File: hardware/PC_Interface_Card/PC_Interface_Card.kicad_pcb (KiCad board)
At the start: 2 copper layers, 69 parts, among them J1 GSB1C41110SSHR, J2 Conn_01x10_Pin, J3 DM3BT-DSF-PEJS, Q1 PMOS, SW1 B3W-900-1, SW2 B3W-900-1, SW3 B3W-900-1, SW4 B3W-900-1, SW5 B3W-900-1, SW6 TL1240YQ2JBLK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

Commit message: footprint and 3d model fixes, footprint mismatch persists for B3W-9000 still. Need a fix.
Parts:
- SW1, SW2, SW3, SW4, SW5: footprint Footprint:B3W-900-1_OMR -> Footprint:SW6_B3W-9-1_OMR
- moved SW1 9.30 mm to (21.7, 23.6)
- moved SW2 9.30 mm to (21.7, 37.5)
- moved SW3 9.30 mm to (21.7, 51.4)
- moved SW4 9.30 mm to (21.7, 65.2)
- moved SW5 9.30 mm to (21.7, 79.1)

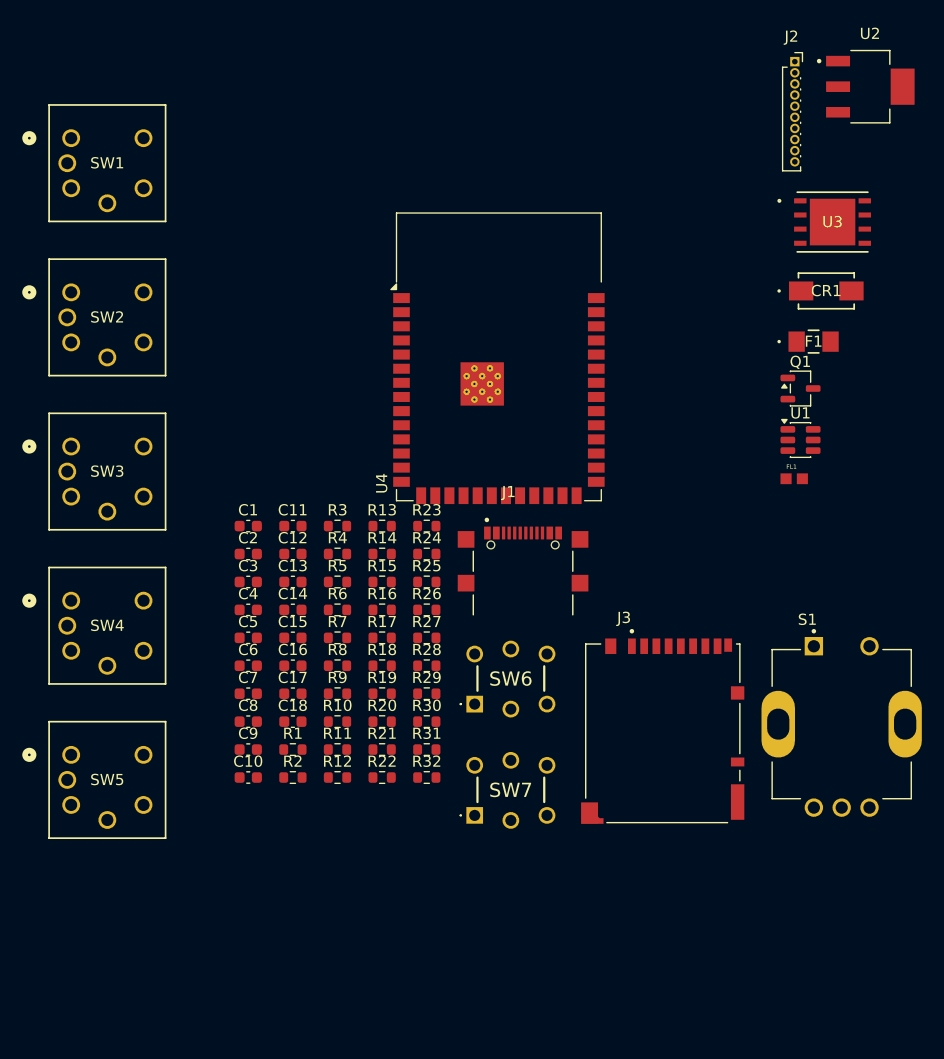
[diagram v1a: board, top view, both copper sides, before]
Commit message: Footprints added with BoM update and all 3d models added.
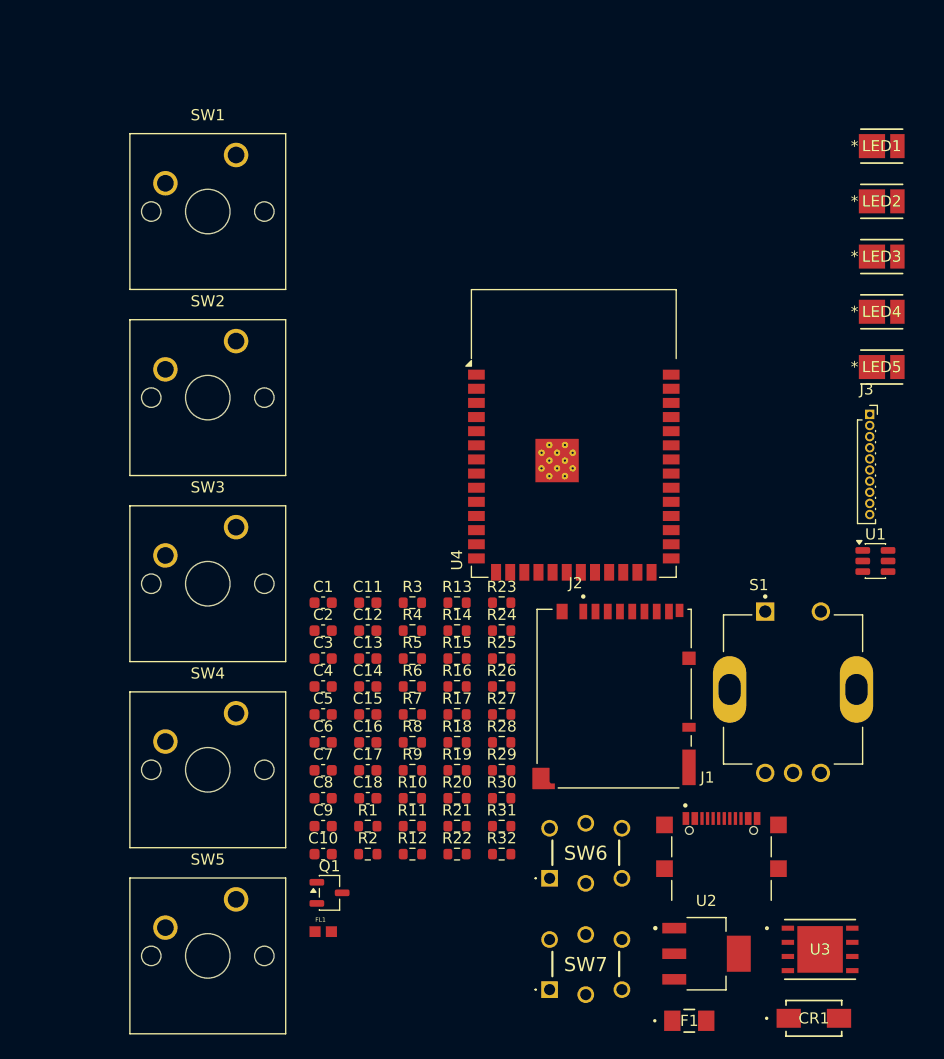
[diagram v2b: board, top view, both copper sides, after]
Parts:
- added LED1: LED_Cree_JE2835, Footprint:LED_JE2835_CRW-M, F.Cu at (94.5, 24.4)
- added LED2: LED_Cree_JE2835, Footprint:LED_JE2835_CRW-M, F.Cu at (94.5, 29.3)
- added LED3: LED_Cree_JE2835, Footprint:LED_JE2835_CRW-M, F.Cu at (94.5, 34.3)
- added LED4: LED_Cree_JE2835, Footprint:LED_JE2835_CRW-M, F.Cu at (94.5, 39.3)
- added LED5: LED_Cree_JE2835, Footprint:LED_JE2835_CRW-M, F.Cu at (94.5, 44.2)
- C10, C14, C5: value 1u_16V_0603 -> 100n_16V_0603
- C13, C16, C3: value 100n_16V_0603 -> 1u_16V_0603
- J2: value Conn_01x10_Pin -> DM3BT-DSF-PEJS; footprint Connector_PinSocket_1.00mm:PinSocket_1x10_P1.00mm_Vertical -> Footprint_Project_PC_Interface:HRS_DM3BT-DSF-PEJS
- J3: value DM3BT-DSF-PEJS -> Conn_01x10_Pin; footprint Footprint_Project_PC_Interface:HRS_DM3BT-DSF-PEJS -> Connector_PinSocket_1.00mm:PinSocket_1x10_P1.00mm_Vertical
- R10, R9: value 5.1k_0.2W_0603 -> 10k_0.2W_0603
- R13, R14, R16, R20, R21, R24: value 68R_0.2W_0603 -> 10k_0.2W_0603
- R17, R19, R22, R23, R26: value 10k_0.2W_0603 -> 33R_0.2W_0603
- R2: value 4R7_0.2W_0603 -> 10k_0.2W_0603
- R27: value 10k_0.2W_0603 -> 68R_0.2W_0603
- R6, R7: value 10k_0.2W_0603 -> 5.1k_0.2W_0603
- R8: value 10k_0.2W_0603 -> 4R7_0.2W_0603
- SW1, SW2, SW3, SW4, SW5: value B3W-900-1 -> CherryMX; footprint Footprint:SW6_B3W-9-1_OMR -> CherryMX_PCB:CherryMX_1.00u_PCB
- moved U2 79.3 mm to (78.8, 96.9)
- moved CR1 65.4 mm to (88.4, 102.7)
- moved U3 65.4 mm to (89.0, 96.5)
- moved F1 62.0 mm to (77.2, 103.0)
- moved Q1 62.0 mm to (44.9, 91.5)
- moved FL1 58.7 mm to (44.3, 94.9)
- moved J2 52.7 mm to (70.5, 66.9)
- moved J1 31.2 mm to (80.1, 88.5)
- moved J3 28.5 mm to (93.4, 48.5)
- moved SW5 21.8 mm to (34.0, 97.1)
- moved SW4 19.5 mm to (34.0, 80.4)
- moved SW3 17.4 mm to (34.0, 63.7)
- moved SW6 17.0 mm to (64.7, 90.2)
- moved SW7 17.0 mm to (64.7, 100.2)
- moved SW2 15.5 mm to (34.0, 47.0)
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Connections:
- C10 pad 1: VCC -> ENC_A
- C11 pad 1: VCC -> ENC_B
- C12 pad 1: SW_EN -> SW_MENU
- C13 pad 1: ENC_SW -> VCC
- C14 pad 1: VCC -> SW_EN
- C16 pad 1: SW_BOOT -> VCC
- C17 pad 1: ENC_A -> SW_BOOT
- C18 pad 1: ENC_B -> VCC
- C3 pad 1: SW_LEFT -> VLDO
- C4 pad 1: SW_UP -> VLDO
- C5 pad 1: VLDO -> SW_LEFT
- C6 pad 1: VLDO -> SW_UP
- C7 pad 1: SW_MENU -> ENC_SW
- J2 pad 1: VCC -> D2_SDMMC
- J2 pad 2: DC_DISP -> D3_SDMMC
- J2 pad 3: CS_DISP -> CMD_SDMMC
- J2 pad 4: MOSI -> VCC
- J2 pad 5: SCLK -> CLK_SDMMC
- J2 pad 6: MISO -> GND
- J2 pad 7: RST_DISP -> D0_SDMMC
- J2 pad 8: LED_DISP -> D1_SDMMC
- J3 pad 1: D2_SDMMC -> VCC
- J3 pad 2: D3_SDMMC -> DC_DISP
- J3 pad 3: CMD_SDMMC -> CS_DISP
- J3 pad 4: VCC -> MOSI
- J3 pad 5: CLK_SDMMC -> SCLK
- J3 pad 6: GND -> MISO
- J3 pad 7: D0_SDMMC -> RST_DISP
- J3 pad 8: D1_SDMMC -> LED_DISP
- R10 pad 1: CC2 -> RST_DISP
- R10 pad 2: GND -> VCC
- R13 pad 1: Net-(SW1-ANODE) -> ENC_SW
- R14 pad 1: Net-(SW2-ANODE) -> SW_RIGHT
- R15 pad 1: SW_MENU -> SW_DN
- R16 pad 1: Net-(SW3-ANODE) -> Net-(U3-*WP)
- R17 pad 1: Net-(U3-*WP) -> Net-(LED1-Pad2)
- R18 pad 1: SW_RIGHT -> ENC_A
- R19 pad 1: SW_DN -> Net-(LED2-Pad2)
- R2 pad 1: LED_DISP -> D1_SDMMC
- R2 pad 2: Net-(Q1-D) -> VCC
- R20 pad 1: Net-(SW4-ANODE) -> ENC_B
- R21 pad 1: Net-(SW5-ANODE) -> SW_MENU
- R22 pad 1: GND -> Net-(LED3-Pad2)
- R22 pad 2: Net-(U3-*RESET) -> VCC
- R23 pad 1: SW_EN -> Net-(LED4-Pad2)
- R24 pad 1: Net-(SW6-+) -> GND
- R24 pad 2: VCC -> Net-(U3-*RESET)
- R25 pad 1: ENC_SW -> SW_EN
- R26 pad 1: GND -> Net-(LED5-Pad2)
- R26 pad 2: Net-(U4-IO3) -> VCC
- R27 pad 1: ENC_A -> Net-(SW6-+)
- R28 pad 1: SW_BOOT -> GND
- R28 pad 2: VCC -> Net-(U4-IO3)
- R29 pad 1: ENC_B -> SW_BOOT
- R3 pad 1: D1_SDMMC -> D2_SDMMC
- R4 pad 1: D2_SDMMC -> D3_SDMMC
- R5 pad 1: D3_SDMMC -> CMD_SDMMC
- R6 pad 1: GND -> CC1
- R6 pad 2: PWM_DISP -> GND
- R7 pad 1: CMD_SDMMC -> CC2
- R7 pad 2: VCC -> GND
- R8 pad 1: RST_DISP -> LED_DISP
- R8 pad 2: VCC -> Net-(Q1-D)
- R9 pad 1: CC1 -> GND
- R9 pad 2: GND -> PWM_DISP
- SW1 pad 2: SW_LEFT -> GND
- SW2 pad 2: SW_UP -> GND
- SW3 pad 1: SW_MENU -> SW_RIGHT
- SW3 pad 2: SW_MENU -> GND
- SW4 pad 1: SW_RIGHT -> SW_DN
- SW4 pad 2: SW_RIGHT -> GND
- SW5 pad 1: SW_DN -> SW_MENU
- SW5 pad 2: SW_DN -> GND

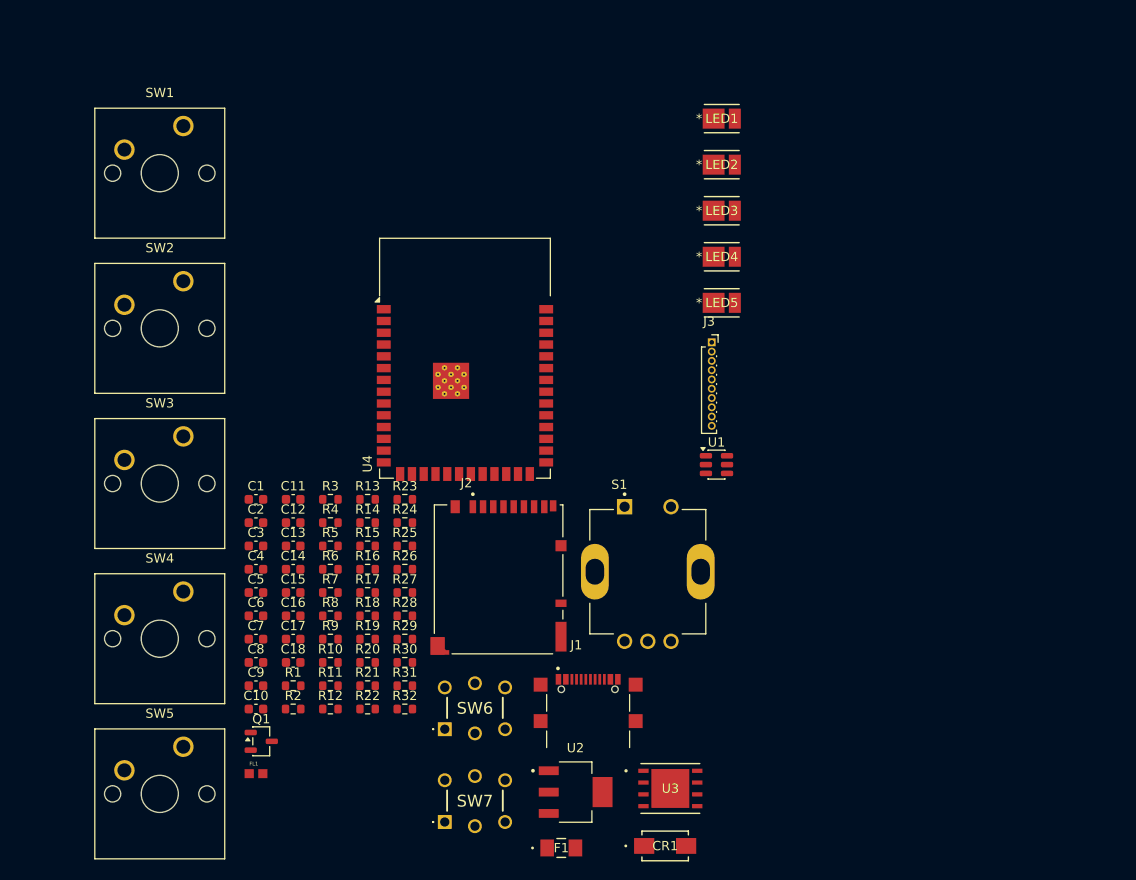
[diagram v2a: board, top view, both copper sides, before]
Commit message: More BoM fixes and 3D models, off board parts added.
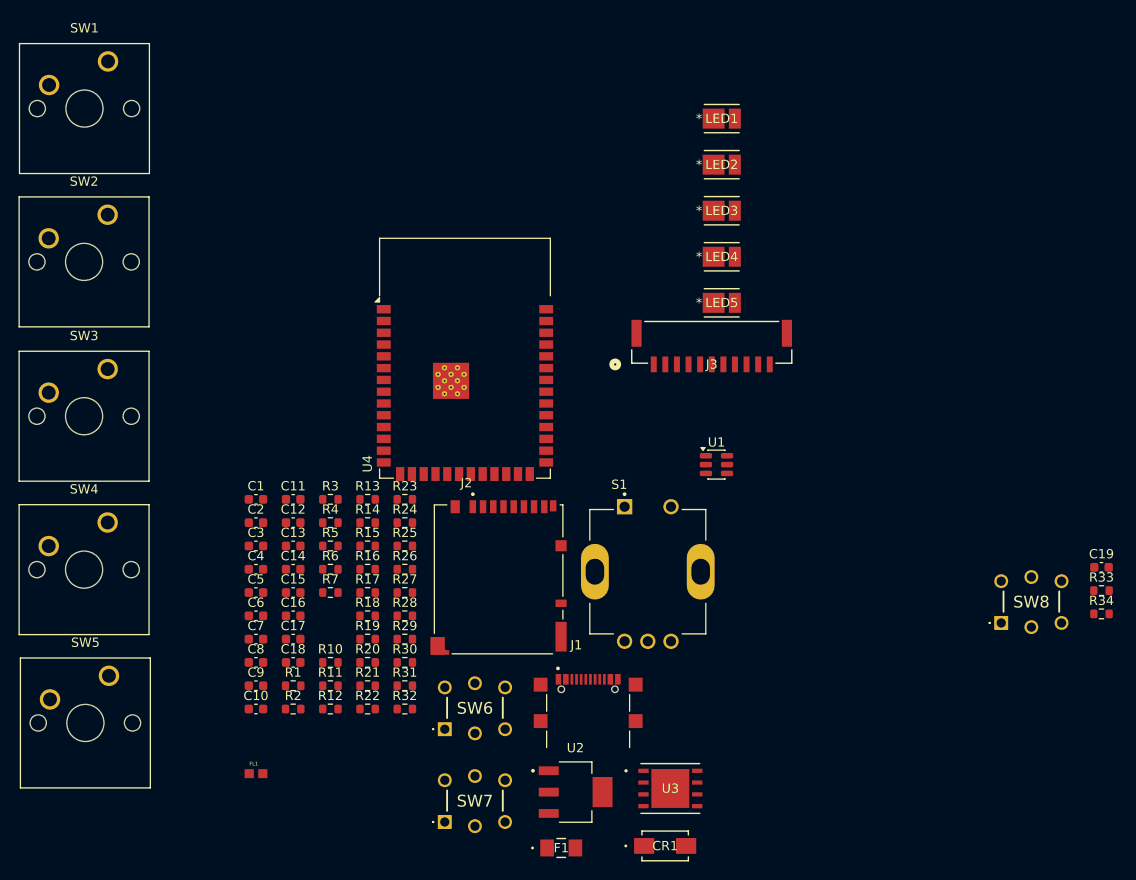
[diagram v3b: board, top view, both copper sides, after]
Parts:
- removed Q1: PMOS, Package_TO_SOT_SMD:SOT-23-3
- removed R8: 4R7_0.2W_0603, Resistor_SMD:R_0603_1608Metric
- removed R9: 10k_0.2W_0603, Resistor_SMD:R_0603_1608Metric
- added C19: 100n_16V_0603, Capacitor_SMD:C_0603_1608Metric, F.Cu at (135.4, 72.7)
- added R33: 10k_0.2W_0603, Resistor_SMD:R_0603_1608Metric, F.Cu at (135.4, 75.2)
- added R34: 68R_0.2W_0603, Resistor_SMD:R_0603_1608Metric, F.Cu at (135.4, 77.7)
- added SW8: TL1240YQ2JBLK, Footprint:TL1240YQ, F.Cu at (124.6, 78.7)
- J3: value Conn_01x10_Pin -> BM11B-GHS-TBT; footprint Connector_PinSocket_1.00mm:PinSocket_1x10_P1.00mm_Vertical -> Footprint_Project_PC_Interface:CONN11_BM11B-GHS-TBTLFSNN_JST
- moved SW5 11.1 mm to (25.9, 89.5)
- moved SW4 11.0 mm to (25.8, 73.0)
- moved SW3 10.9 mm to (25.8, 56.4)
- moved SW2 10.9 mm to (25.8, 39.8)
- moved SW1 10.7 mm to (25.9, 23.3)
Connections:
- J3 pad 2: DC_DISP -> GND
- J3 pad 3: CS_DISP -> MISO
- J3 pad 6: MISO -> CS_DISP
- J3 pad 7: RST_DISP -> DC_DISP
- J3 pad 8: LED_DISP -> RST_DISP
- J3 pad 9: GND -> PWM_DISP

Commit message: Changed encoder to a right angle one
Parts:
- removed S1: PEC11R-4120K-S0018, Footprint:XDCR_PEC11R-4120K-S0018
- added MT1: ACZ11BR1E-15KQA1-12C, Footprint:XDCR_ACZ11BR1E-15KQA1-12C, F.Cu at (231.2, 33.9)
- moved U2 113.1 mm to (13.4, 4.64)
- moved U4 107.0 mm to (167.2, 13.2)
- moved SW6 105.2 mm to (168.9, 104.6)
- moved U3 104.6 mm to (-3.50, 47.7)
- moved J3 92.7 mm to (185.1, 62.4)
- moved CR1 92.1 mm to (-3.14, 92.6)
- moved U1 90.9 mm to (26.2, 1.04)
- moved F1 84.8 mm to (-2.98, 75.5)
- moved C1 82.9 mm to (45.5, -17.5)
- moved C11 82.9 mm to (49.5, -17.5)
- moved C13 82.9 mm to (49.5, -12.5)
- moved C16 82.9 mm to (49.5, -4.98)
- moved C3 82.9 mm to (45.5, -12.5)
- moved C6 82.9 mm to (45.5, -4.98)
- moved C9 82.9 mm to (45.5, 2.55)
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
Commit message: footprint fixes
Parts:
- SW7, SW8: moved to B.Cu
- moved MT1 317.5 mm to (-80.9, -24.4), turned to 180 degrees
- moved SW6 282.0 mm to (-96.1, 7.98)
- moved SW8 276.4 mm to (-104.2, -13.3), turned to 180 degrees
- moved SW7 273.2 mm to (-114.4, -13.3), turned to 180 degrees
- moved J3 261.8 mm to (-69.4, 0.85), turned to 90 degrees
- moved LED1 260.2 mm to (-131.8, 29.8), turned to 180 degrees
- moved C19 251.3 mm to (-52.0, 25.4)
- moved R33 251.3 mm to (-52.0, 27.9)
- moved R34 251.3 mm to (-52.0, 30.4)
- moved LED4 242.0 mm to (-112.5, 49.2), turned to 180 degrees
- moved LED3 239.6 mm to (-112.6, 29.9), turned to 180 degrees
- moved LED2 238.1 mm to (-112.6, 10.5), turned to 180 degrees
- moved LED5 219.3 mm to (-93.4, 29.8), turned to 180 degrees
- moved U4 218.8 mm to (-49.1, -19.6)
- moved J2 212.5 mm to (-125.9, 42.4), turned to -90 degrees
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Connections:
- C17 pad 1: SW_BOOT -> SW_EN
- J3 pad 12: (no net) -> GND
- J3 pad 13: (no net) -> GND
- R29 pad 1: SW_BOOT -> SW_EN
- SW7 pad 1: SW_BOOT -> SW_EN
- SW7 pad 2: SW_BOOT -> SW_EN

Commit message: Added via and trace rules
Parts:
- moved J2 225.4 mm to (91.5, 102.1), turned to 0 degrees
- moved U2 200.8 mm to (118.5, 93.1)
- moved F1 196.9 mm to (127.4, 81.1)
- moved J1 183.0 mm to (129.1, 73.0)
- moved U1 176.5 mm to (121.9, 51.0), turned to 180 degrees
- moved LED1 176.4 mm to (32.3, 94.3)
- moved LED2 176.4 mm to (51.6, 75.0)
- moved LED3 176.4 mm to (51.6, 94.4)
- moved LED4 176.4 mm to (51.7, 113.7)
- moved LED5 176.4 mm to (70.8, 94.3)
- moved SW2 176.4 mm to (51.6, 69.9)
- moved SW3 176.4 mm to (70.9, 89.3)
- moved SW4 176.4 mm to (51.6, 108.6)
- moved SW5 176.4 mm to (51.6, 89.3)
- moved SW6 176.4 mm to (68.1, 72.5)
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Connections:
- C14 pad 1: SW_EN -> SW_PLAY
- R25 pad 1: SW_EN -> SW_PLAY
- SW6 pad 1: SW_EN -> SW_PLAY
- SW6 pad 2: SW_EN -> SW_PLAY
- U4 pad 36: unconnected-(U4-RXD0-Pad36) -> SW_PLAY

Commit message: Start of day work - 24/01
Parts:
- added H1: MountingHole_Pad, MountingHole:MountingHole_2.2mm_M2_Pad_Via, F.Cu at (-31.5, 19.7)
- added H10: MountingHole_Pad, MountingHole:MountingHole_2.2mm_M2_Pad_Via, F.Cu at (-25.6, 43.5)
- added H2: MountingHole_Pad, MountingHole:MountingHole_2.2mm_M2_Pad_Via, F.Cu at (-31.5, 25.6)
- added H3: MountingHole_Pad, MountingHole:MountingHole_2.2mm_M2_Pad_Via, F.Cu at (-31.5, 31.6)
- added H4: MountingHole_Pad, MountingHole:MountingHole_2.2mm_M2_Pad_Via, F.Cu at (-31.5, 37.5)
- added H5: MountingHole_Pad, MountingHole:MountingHole_2.2mm_M2_Pad_Via, F.Cu at (-31.5, 43.5)
- added H6: MountingHole_Pad, MountingHole:MountingHole_2.2mm_M2_Pad_Via, F.Cu at (-25.6, 19.7)
- added H7: MountingHole_Pad, MountingHole:MountingHole_2.2mm_M2_Pad_Via, F.Cu at (-25.6, 25.6)
- added H8: MountingHole_Pad, MountingHole:MountingHole_2.2mm_M2_Pad_Via, F.Cu at (-25.6, 31.6)
- added H9: MountingHole_Pad, MountingHole:MountingHole_2.2mm_M2_Pad_Via, F.Cu at (-25.6, 37.5)
- moved C14 37.7 mm to (45.8, 48.8)
- moved R25 37.7 mm to (49.0, 48.8)
- moved R27 37.7 mm to (49.0, 50.4)
- moved SW6 37.7 mm to (41.6, 45.6)
- moved SW2 23.2 mm to (48.7, 93.0)
- moved LED2 23.0 mm to (48.9, 97.9)
- moved SW3 21.8 mm to (66.2, 110.6)
- moved LED5 21.6 mm to (66.5, 115.5)
- moved C12 21.5 mm to (37.4, 98.6)
- moved C8 21.5 mm to (65.1, 122.9)
- moved C9 21.5 mm to (37.5, 129.1)
- moved R23 21.5 mm to (48.3, 140.5)
- moved C5 21.5 mm to (26.4, 98.5)
- moved C6 21.5 mm to (37.6, 90.3)
- moved LED3 21.5 mm to (48.8, 115.7)
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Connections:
- net VLDO renamed VLDO_In
- C1 pad 1: VCC -> 3V3
- C13 pad 1: VCC -> 3V3
- C15 pad 1: VCC -> 3V3
- C16 pad 1: VCC -> 3V3
- C18 pad 1: VCC -> 3V3
- C2 pad 1: VCC -> 3V3
- J2 pad 4: VCC -> 3V3
- J3 pad 1: VCC -> 3V3
- R1 pad 2: VCC -> 3V3
- R10 pad 2: VCC -> 3V3
- R11 pad 2: VCC -> 3V3
- R12 pad 2: VCC -> 3V3
- R13 pad 2: VCC -> unconnected-(R13-Pad2)
- R14 pad 2: VCC -> 3V3
- R15 pad 2: VCC -> 3V3
- R16 pad 2: VCC -> 3V3
- R17 pad 2: VCC -> 3V3
- R18 pad 2: VCC -> unconnected-(R18-Pad2)
- R19 pad 2: VCC -> 3V3
- R2 pad 2: VCC -> 3V3
- R20 pad 2: VCC -> unconnected-(R20-Pad2)
- R21 pad 2: VCC -> 3V3
- R22 pad 2: VCC -> 3V3
- R23 pad 2: VCC -> 3V3
- R25 pad 2: VCC -> 3V3
- R26 pad 2: VCC -> 3V3
- R27 pad 2: VCC -> 3V3
- R29 pad 2: VCC -> 3V3
- R3 pad 2: VCC -> 3V3
- R30 pad 2: VCC -> 3V3
- R33 pad 2: VCC -> 3V3
- R34 pad 2: VCC -> 3V3
- R4 pad 2: VCC -> 3V3
- R5 pad 2: VCC -> 3V3
- U2 pad 2: VCC -> 3V3
- U2 pad 4: VCC -> 3V3
- U3 pad 8: VCC -> 3V3
- U4 pad 2: VCC -> 3V3
